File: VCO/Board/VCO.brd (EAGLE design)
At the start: 101.3 x 49.5 mm, 62 parts, among them IC1 AD711N, IC2 AD711N, IC3 AD711N, IC4 AD711N, IC5 AD711N, T1 BC337, T2 BC337

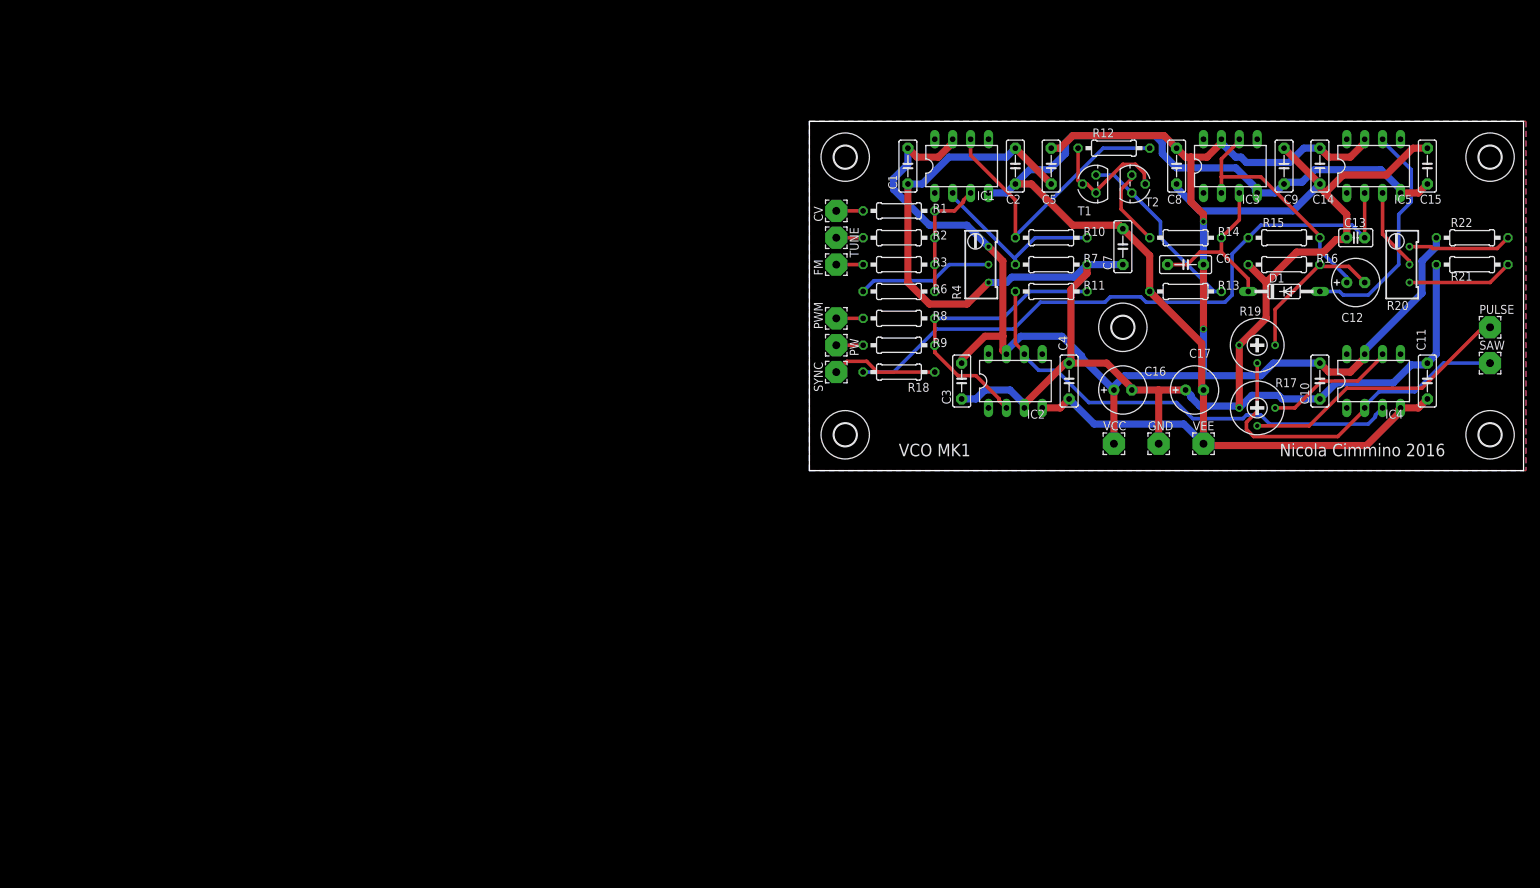
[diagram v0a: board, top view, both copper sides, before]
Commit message: Change VCO connectors
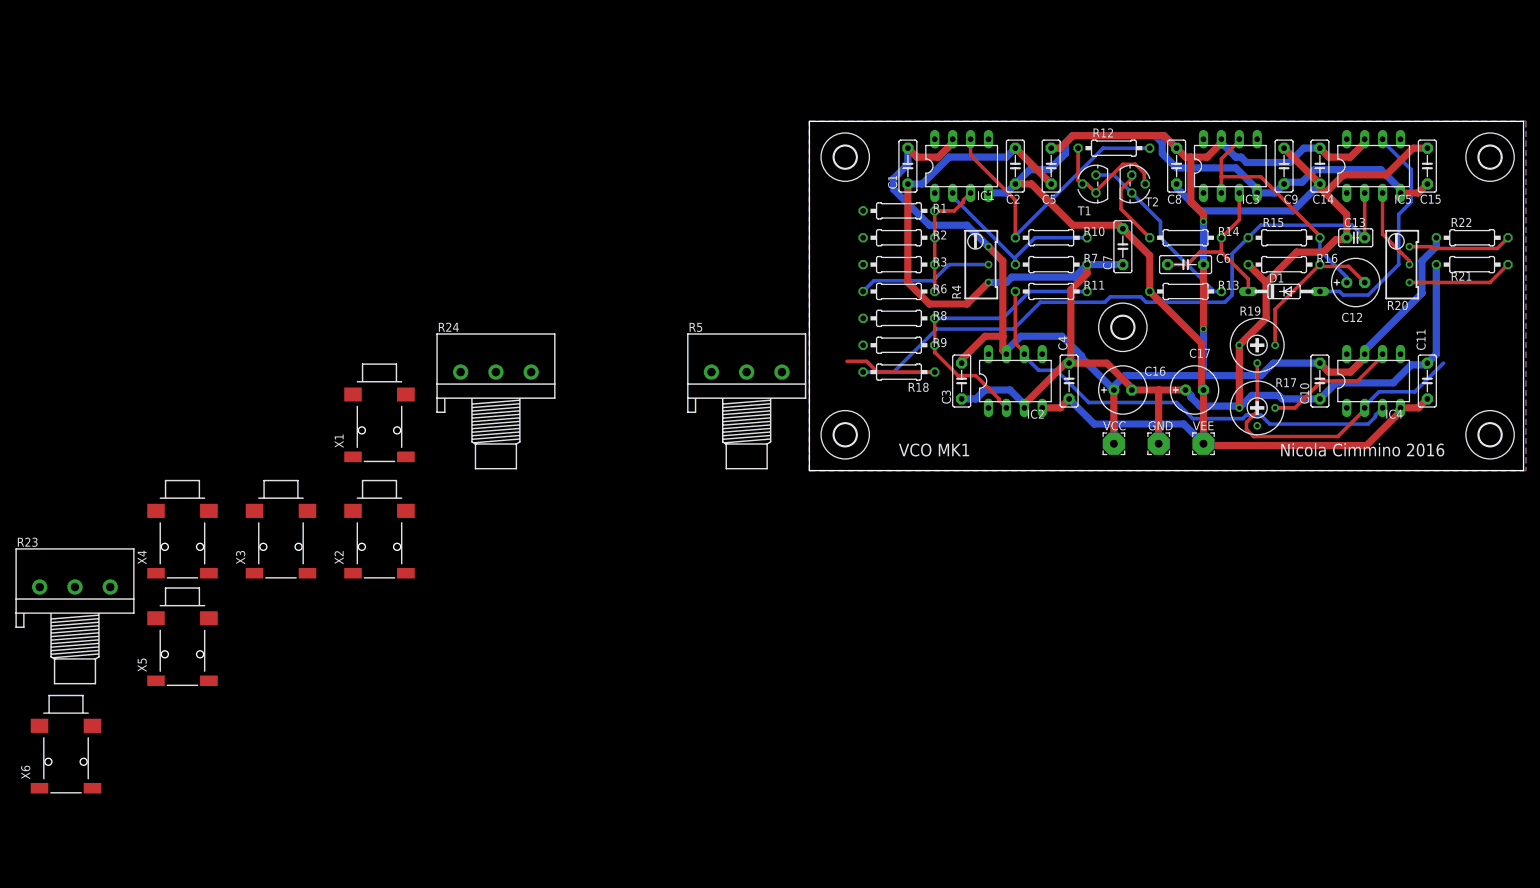
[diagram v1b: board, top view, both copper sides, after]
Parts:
- removed CV, FM, PULSE, PW, PWM, SAW, SYNC, TUNE: (no value), wirepad:3,17/1,1
- added R23, R24, R5: 10k, pot:3RP/1610N
- added X1, X2, X3, X4, X5, X6: 1503_02, con-lumberg:1503_02
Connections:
- new net N$26: R24.3, X2.2, X2.3
- net GND: now also R23.1, R24.1, R5.1, X1.1, X2.1, X3.1, X4.1, X5.1, X6.1
- net N$12: now also X1.2, X1.3; no longer CV.1
- net N$14: now also R24.2; no longer FM.1
- net N$15: now also X6.2, X6.3; no longer SYNC.1
- net N$17: now also R5.2; no longer TUNE.1
- net N$21: now also X4.2, X4.3; no longer SAW.1
- net N$23: now also X3.3; no longer PULSE.1
- net N$27: now also R23.2; no longer PWM.1
- net N$28: now also X5.2, X5.3; no longer PW.1
- net VCC: now also R23.3, R5.3
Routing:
- net N$23: track 38.8 -> 0.00 mm
- net N$21: track 49.6 -> 43.0 mm
- net N$28: track 3.81 -> 0.00 mm
- net N$27: track 3.81 -> 0.00 mm
- net N$17: track 3.81 -> 0.00 mm
- net N$14: track 3.81 -> 0.00 mm
- net N$12: track 3.81 -> 0.00 mm
- net N$15: track 15.2 -> 13.1 mm

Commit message: Change VCO to use TL074
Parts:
- removed C14, C15, C3, C4, C8, C9: 100n, capacitor-wima:C5B2.5
- removed IC2, IC3, IC5: AD711N, analog-devices:DIL08
- IC1: value AD711N -> TL074P; device analog-devices:DIL08 -> linear:DIL14
- moved IC1 155.7 mm to (-101.6, -31.8)
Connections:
- new net V+: IC1.4
- new net V-: IC1.11
- net GND: now also IC1.10; no longer C14.1, C15.2, C3.1, C4.2, C8.1, C9.2, IC2.3
- net N$18: now also IC1.1; no longer IC1.6
- net N$24: now also IC1.9; no longer IC2.2
- net N$29: now also IC1.8; no longer IC2.6
- net N$3: now also IC1.5; no longer IC3.3
- net N$5: now also IC1.14; no longer IC5.6
- net N$6: now also IC1.12; no longer IC5.3
- net N$7: now also IC1.13; no longer IC5.2
- net N$8: now also IC1.6, IC1.7; no longer IC3.2, IC3.6
- net VCC: no longer C14.2, C3.2, C8.2, IC1.7, IC2.7, IC3.7, IC5.7
- net VEE: no longer C15.1, C4.1, C9.1, IC1.4, IC2.4, IC3.4, IC5.4
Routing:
- net GND: track 281.0 -> 221.9 mm
- net VEE: track 188.6 -> 148.6 mm
- net VCC: track 227.2 -> 195.4 mm
- net N$7: track 90.9 -> 84.5 mm
- net N$6: track 11.7 -> 5.90 mm
- net N$3: track 25.0 -> 21.1 mm
- net N$8: track 34.3 -> 31.8 mm
- net N$18: track 41.1 -> 38.8 mm
- net N$24: track 41.6 -> 40.1 mm
- net N$13: track 17.7 -> 16.3 mm
- net N$29: track 66.0 -> 65.5 mm
- net N$20: track 25.3 -> 24.8 mm

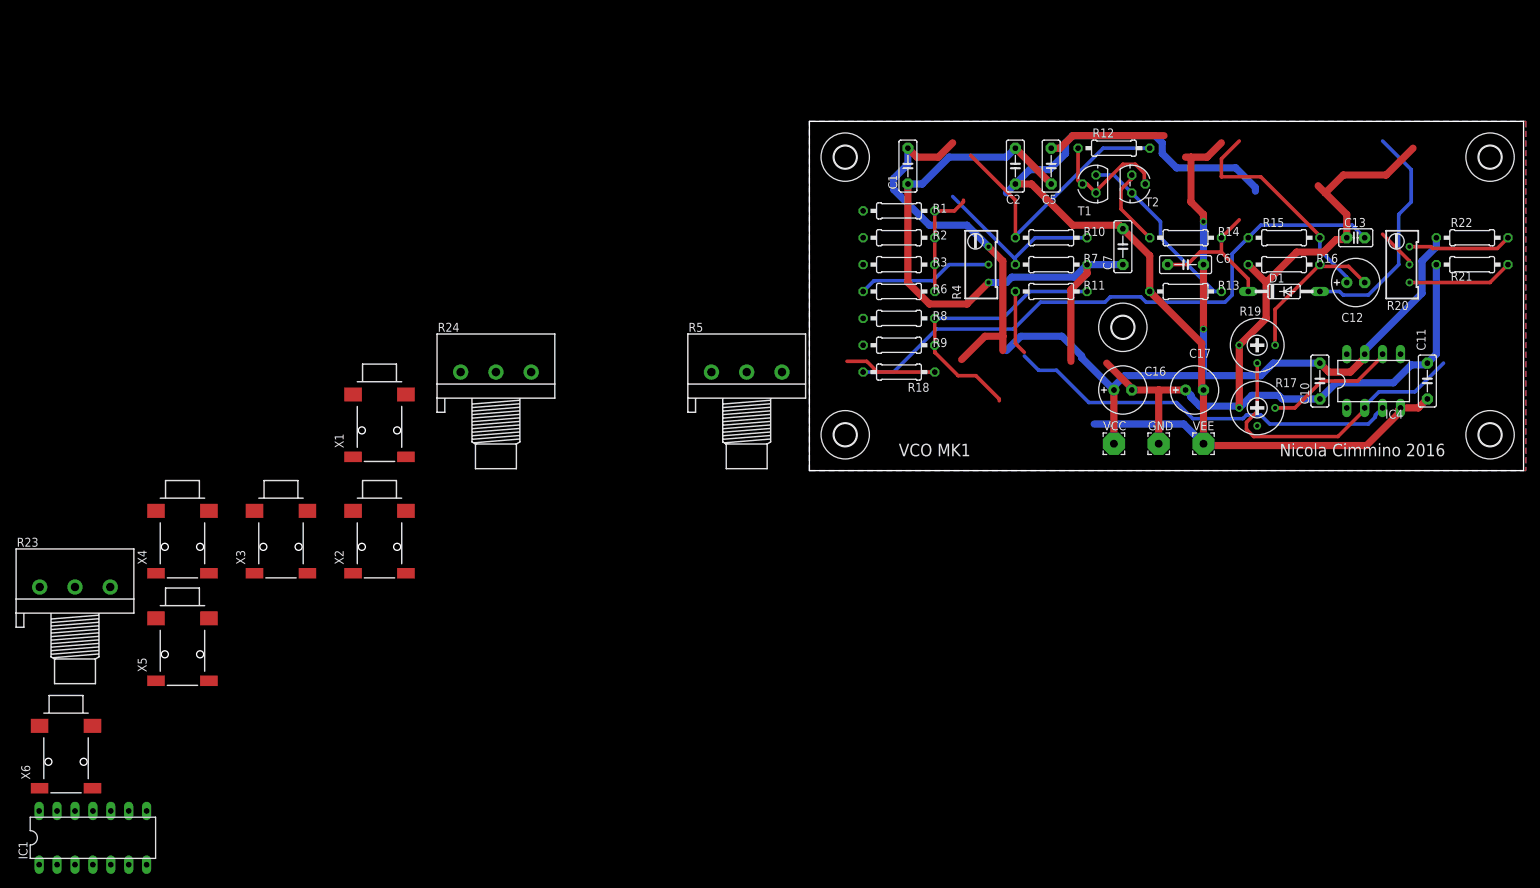
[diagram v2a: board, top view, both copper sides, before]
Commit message: Tweks to reduce BOM cost
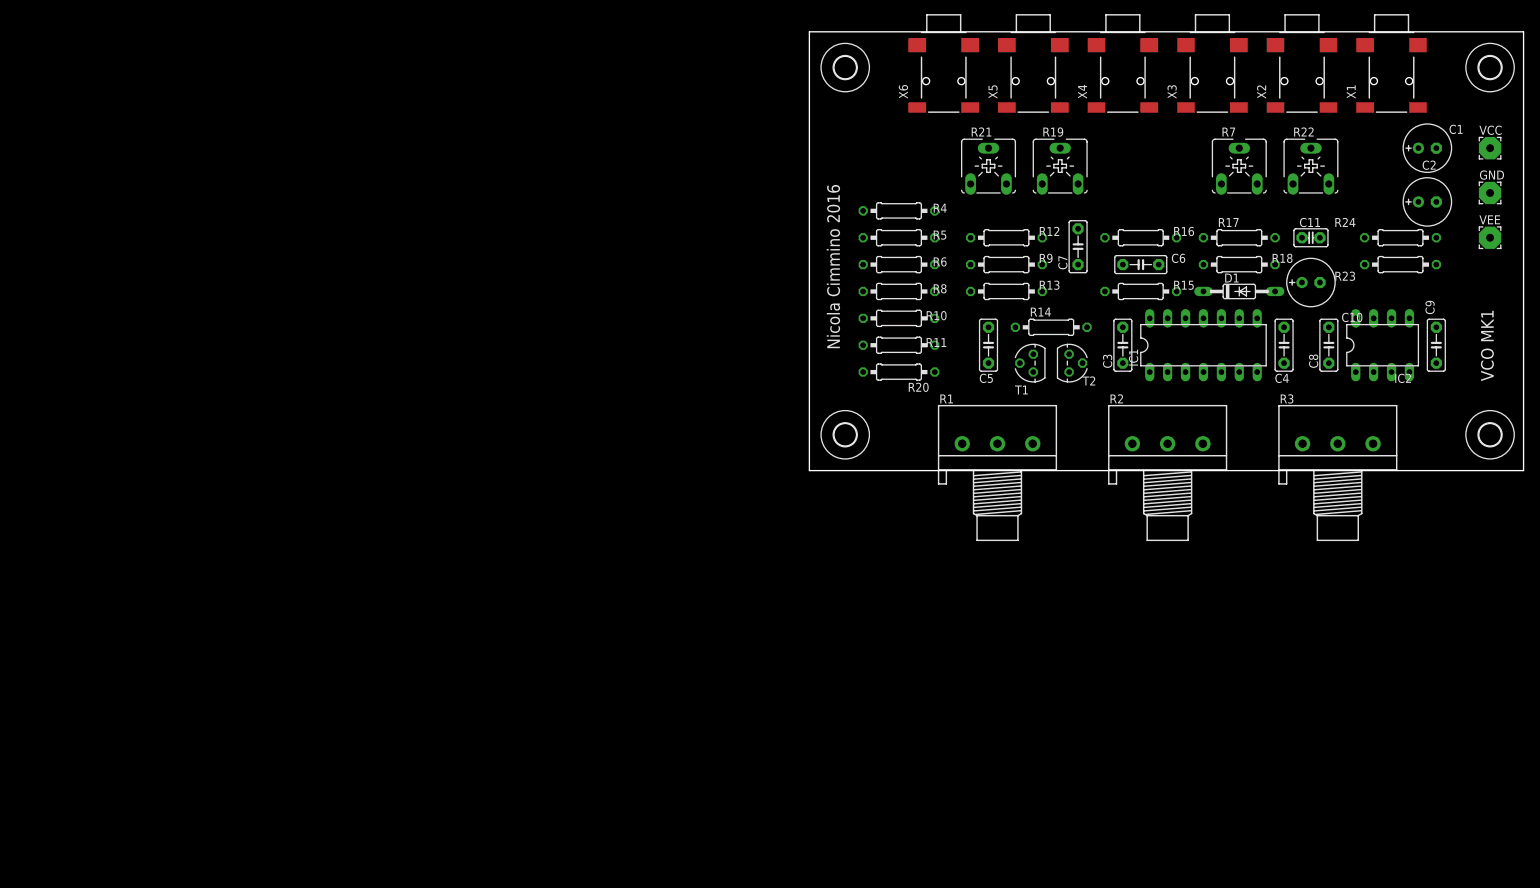
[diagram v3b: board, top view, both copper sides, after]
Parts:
- removed C12, C16, C17: 10u, rcl:E2,5-7
- removed C13: 100p, capacitor-wima:C2.5-2
- removed IC4: AD711N, analog-devices:DIL08
- removed U$5: (no value), holes:3,2
- added C3, C4, C8, C9: 100n, capacitor-wima:C5B2.5
- added IC2: AD711N, analog-devices:DIL08
- C1, C10, C2: value 100n -> 10u; device capacitor-wima:C5B2.5 -> rcl:E2,5-7
- C11: value 100n -> 100p; device capacitor-wima:C5B2.5 -> capacitor-wima:C2.5-2
- R1, R2, R3: value 100k -> 10k; device eagle-ltspice:0207/10 -> pot:3RP/1610N
- R12: value 27K -> 100k
- R13: value 0R -> 100k
- R14: value 10K -> 27K
- R15: value 100K -> 0R
- R17: value 10k -> 100K; device resistor:RTRIM3339P -> eagle-ltspice:0207/10
- R18: value 1K -> 10K
- R19: value 10k -> 10K; device resistor:RTRIM3339P -> pot:CA6V
- R20: value 47k -> 1K; device rcl:RTRIM64W -> eagle-ltspice:0207/10
- R21, R22: device eagle-ltspice:0207/10 -> pot:CA6V
- R23, R24: value 10k -> 10K; device pot:3RP/1610N -> eagle-ltspice:0207/10
- R4: value 47k -> 100k; device rcl:RTRIM64W -> eagle-ltspice:0207/10
- R5: value 10k -> 100k; device pot:3RP/1610N -> eagle-ltspice:0207/10
- R7: value 100k -> 10K; device eagle-ltspice:0207/10 -> pot:CA6V
- moved R23 193.4 mm to (83.8, 49.5)
- moved IC1 172.3 mm to (55.9, 38.1)
- moved X6 157.5 mm to (19.1, 82.5)
- moved X1 151.8 mm to (82.5, 82.5)
- moved X4 148.8 mm to (44.5, 82.5)
- moved X3 147.7 mm to (57.1, 82.5)
- moved X2 146.5 mm to (69.8, 82.5)
- moved X5 145.5 mm to (31.8, 82.5)
- moved R24 129.7 mm to (83.8, 53.3)
- moved U$3 99.6 mm to (5.08, 25.4)
- moved U$1 92.3 mm to (96.5, 77.5)
- moved C1 73.7 mm to (87.6, 66.0), turned to 0 degrees
- moved R20 72.7 mm to (12.7, 34.3), turned to 180 degrees
- moved R21 70.0 mm to (25.4, 63.5)
- moved VCC 67.8 mm to (96.5, 66.0)
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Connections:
- net GND: now also C1.-, C11.1, C2.+, C3.1, C4.2, C8.1, C9.2, R1.1, R18.1, R19.A, R2.1, R21.A, R3.1, R7.A, R9.2; no longer C1.1, C10.1, C11.2, C13.1, C16.-, C17.+, C2.2, R16.1, R17.1, R19.1, R21.1, R24.1, R4.1, R5.1, R7.2
- net N$1: now also R14.1; no longer R12.1
- net N$10: now also R7.S, R8.2; no longer R4.2, R6.2
- net N$11: now also R22.E, R24.2; no longer R20.3, R22.2
- net N$12: now also R4.2; no longer R1.2
- net N$13: now also R4.1, R5.1, R8.1; no longer R1.1, R2.1, R3.1
- net N$14: now also R2.2, R6.2; no longer R24.2, R3.2
- net N$15: now also R20.1, X4.2, X4.3; no longer R18.1, X6.2, X6.3
- net N$17: now also R1.2; no longer R2.2
- net N$18: now also R12.1, R14.2; no longer R10.1, R12.2
- net N$2: now also R15.2; no longer R13.2
- net N$20: now also R12.2, R9.1; no longer R10.2, R7.1
- net N$21: now also IC2.2, R21.S, X5.2, X5.3; no longer IC4.2, R19.2, X4.2, X4.3
- net N$22: now also IC2.6, R19.E; no longer IC4.6, R17.3
- net N$23: now also R19.S, X6.3; no longer R17.2, X3.3
- net N$24: now also R10.1, R11.1, R13.2; no longer R11.2, R8.1, R9.1
- net N$25: now also C10.-, R18.2, R21.E; no longer C12.-, R16.2, R19.3
- net N$26: now also R2.3; no longer R24.3
- net N$27: now also R10.2, R3.2; no longer R23.2, R8.2
- net N$28: now also R11.2, X3.2, X3.3; no longer R9.2, X5.2, X5.3
- net N$29: now also IC2.3, R13.1; no longer IC4.3, R11.1
- net N$3: now also R16.2; no longer R14.2
- net N$4: now also R16.1; no longer R14.1
- net N$6: now also R22.S; no longer R20.2
- net N$7: now also C11.2, R17.1, R20.2; no longer C13.2, R15.1, R18.2
- net N$8: now also C10.+, R17.2; no longer C12.+, R15.2
- net N$9: now also R22.A, R23.2; no longer R20.1, R21.2
- net VCC: now also C1.+, C3.2, C8.2, IC2.7, R1.3, R24.1, R3.3, R7.E; no longer C1.2, C10.2, C16.+, IC4.7, R22.1, R23.3, R4.3, R5.3
- net VEE: now also C2.-, C4.1, C9.1, IC2.4, R15.1; no longer C11.1, C17.-, C2.1, IC4.4, R13.1
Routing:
- net GND: track 221.9 -> 0.00 mm
- net VCC: track 195.4 -> 0.00 mm, vias 2 -> 0
- net VEE: track 148.6 -> 0.00 mm
- net N$7: track 84.5 -> 0.00 mm
- net N$29: track 65.5 -> 0.00 mm
- net N$21: track 43.0 -> 0.00 mm
- net N$24: track 40.1 -> 0.00 mm
- net N$18: track 38.8 -> 0.00 mm
- net N$5: track 33.1 -> 0.00 mm
- net N$8: track 31.8 -> 0.00 mm
- net N$2: track 26.0 -> 0.00 mm
- net N$20: track 24.8 -> 0.00 mm
- net N$25: track 21.6 -> 0.00 mm
- net N$3: track 21.1 -> 0.00 mm
- net N$10: track 19.4 -> 0.00 mm
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- removed copper zone on layer 1, net N$16
- removed copper zone on layer 16, net N$19
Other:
- board size 101.3 x 49.5 mm -> 101.3 x 62.2 mm

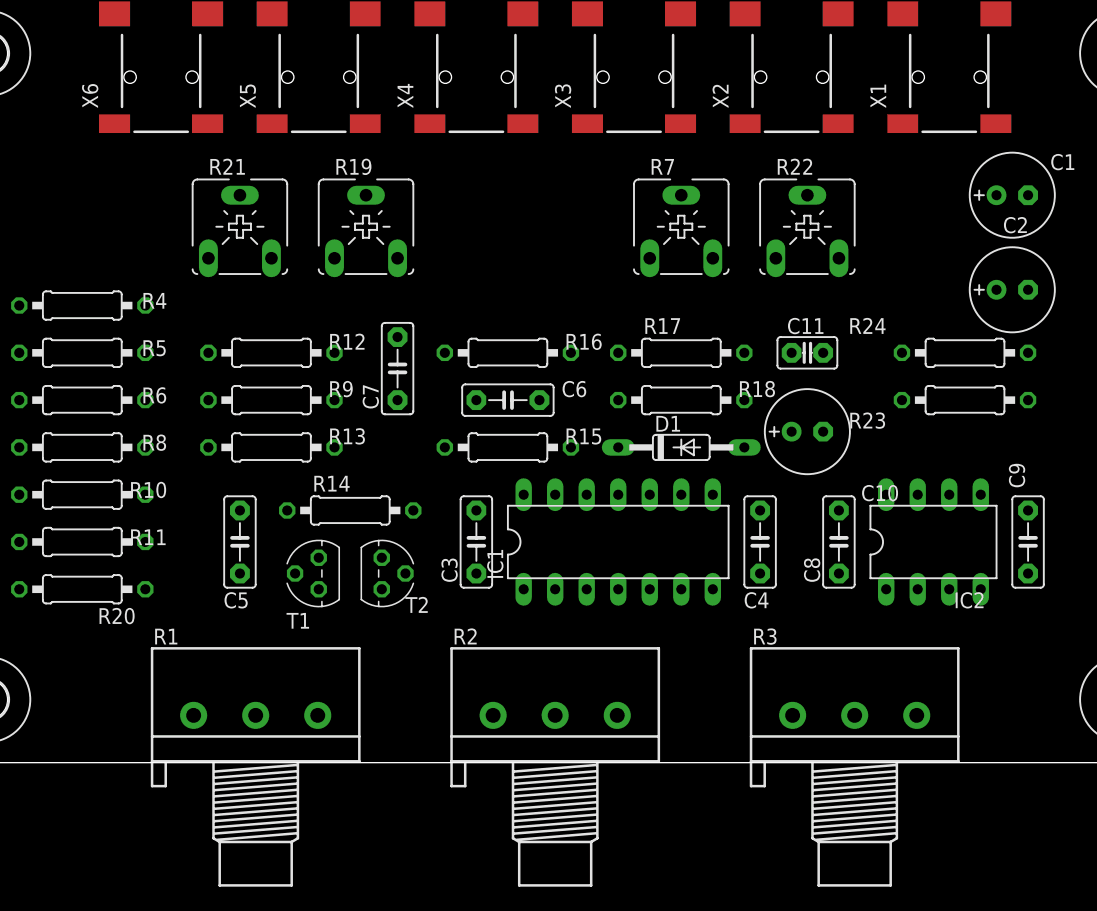
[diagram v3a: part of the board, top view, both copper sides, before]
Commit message: Add PWM pot
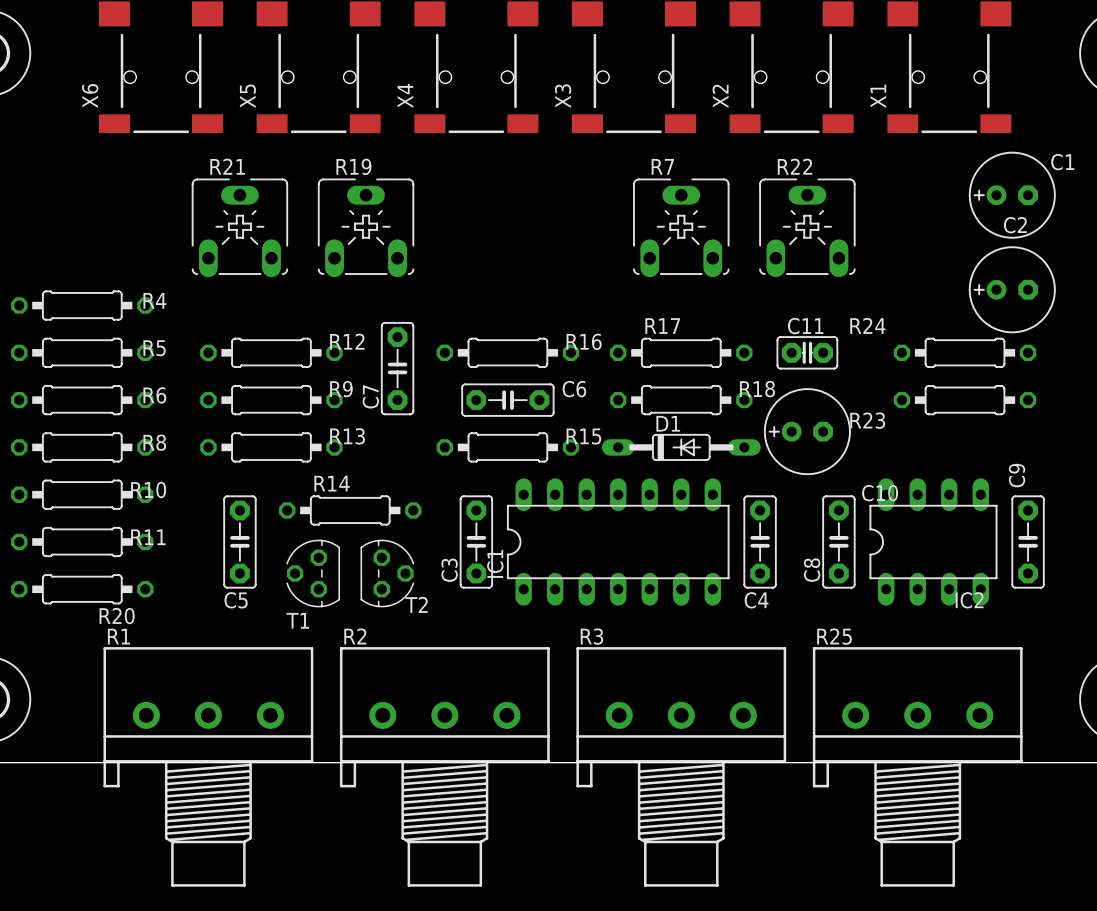
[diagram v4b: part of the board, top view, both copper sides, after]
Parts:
- added R25: 10k, pot:3RP/1610N
- moved R3 14.0 mm to (61.0, 24.1)
- moved R2 8.89 mm to (41.9, 24.1)
- moved R1 3.81 mm to (22.9, 24.1)
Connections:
- new net N$16: R11.2, R25.2
- net GND: now also R25.1
- net N$28: now also R25.3; no longer R11.2
